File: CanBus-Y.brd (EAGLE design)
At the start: 58.4 x 15.9 mm, 3 parts

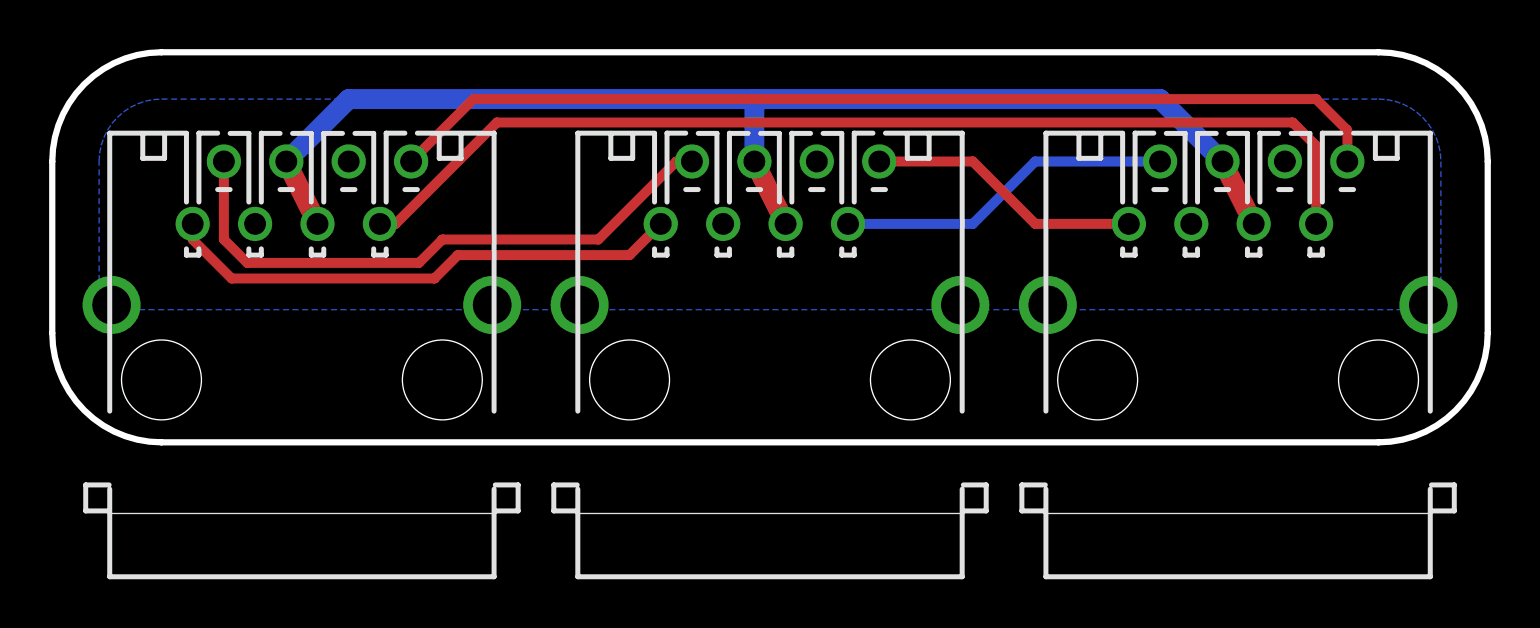
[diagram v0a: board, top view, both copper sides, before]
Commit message: Layouts angepasst, Backplane vergrößert
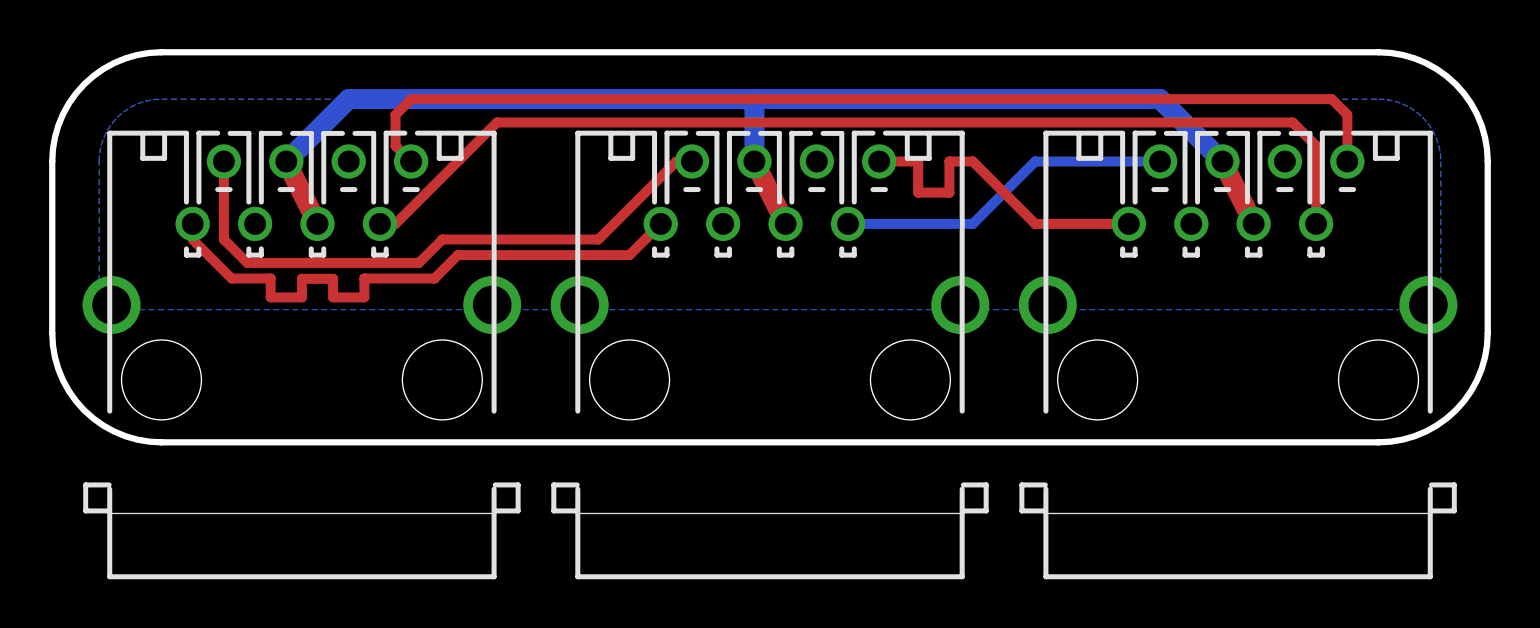
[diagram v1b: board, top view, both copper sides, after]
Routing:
- net CANL_1-2: track 21.3 -> 24.3 mm
- net CANL_2-3: track 11.2 -> 13.8 mm
- net CANL_3-1: track 40.9 -> 43.3 mm
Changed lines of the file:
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@@
 <wire x1="50.8" y1="8.89" x2="50.8" y2="12.065" width="0.4064" layer="1"/>
 <wire x1="50.8" y1="12.065" x2="49.8475" y2="13.0175" width="0.4064" layer="1"/>
-<wire x1="17.4625" y1="13.0175" x2="49.8475" y2="13.0175" width="0.4064" layer="1"/>
+<wire x1="49.8475" y1="13.0175" x2="17.4625" y2="13.0175" width="0.4064" layer="1"/>
 <wire x1="17.4625" y1="13.0175" x2="13.335" y2="8.89" width="0.4064" layer="1"/>
 <wire x1="13.335" y1="8.89" x2="12.7" y2="8.89" width="0.4064" layer="1"/>
@@
 <contactref element="J3" pad="8"/>
 <contactref element="J1" pad="8"/>
-<wire x1="52.07" y1="11.43" x2="52.07" y2="12.7" width="0.4064" layer="1"/>
-<wire x1="52.07" y1="12.7" x2="50.8" y2="13.97" width="0.4064" layer="1"/>
-<wire x1="16.51" y1="13.97" x2="50.8" y2="13.97" width="0.4064" layer="1"/>
-<wire x1="16.51" y1="13.97" x2="13.97" y2="11.43" width="0.4064" layer="1"/>
+<wire x1="52.07" y1="13.335" x2="52.07" y2="11.43" width="0.4064" layer="1"/>
+<wire x1="52.07" y1="13.335" x2="51.435" y2="13.97" width="0.4064" layer="1"/>
+<wire x1="51.435" y1="13.97" x2="13.97" y2="13.97" width="0.4064" layer="1"/>
+<wire x1="13.97" y1="13.97" x2="13.335" y2="13.335" width="0.4064" layer="1"/>
+<wire x1="13.335" y1="13.335" x2="13.335" y2="12.065" width="0.4064" layer="1"/>
+<wire x1="13.335" y1="12.065" x2="13.97" y2="11.43" width="0.4064" layer="1"/>
 </signal>
 <signal name="CANL_1-2">
@@
 <wire x1="5.08" y1="8.89" x2="5.08" y2="8.255" width="0.4064" layer="1"/>
 <wire x1="5.08" y1="8.255" x2="6.6675" y2="6.6675" width="0.4064" layer="1"/>
-<wire x1="6.6675" y1="6.6675" x2="14.9225" y2="6.6675" width="0.4064" layer="1"/>
 <wire x1="14.9225" y1="6.6675" x2="15.875" y2="7.62" width="0.4064" layer="1"/>
 <wire x1="15.875" y1="7.62" x2="22.86" y2="7.62" width="0.4064" layer="1"/>
 <wire x1="22.86" y1="7.62" x2="24.13" y2="8.89" width="0.4064" layer="1"/>
+<wire x1="8.255" y1="6.6675" x2="6.6675" y2="6.6675" width="0.4064" layer="1"/>
+<wire x1="8.255" y1="5.89915" x2="8.255" y2="6.6675" width="0.4064" layer="1"/>
+<wire x1="9.525" y1="5.89915" x2="8.255" y2="5.89915" width="0.4064" layer="1"/>
+<wire x1="9.525" y1="5.89915" x2="9.525" y2="6.6548" width="0.4064" layer="1"/>
+<wire x1="10.795" y1="6.6548" x2="9.525" y2="6.6548" width="0.4064" layer="1"/>
+<wire x1="10.795" y1="6.6548" x2="10.795" y2="5.89915" width="0.4064" layer="1"/>
+<wire x1="10.795" y1="5.89915" x2="12.065" y2="5.89915" width="0.4064" layer="1"/>
+<wire x1="12.065" y1="5.89915" x2="12.065" y2="6.6675" width="0.4064" layer="1"/>
+<wire x1="12.065" y1="6.6675" x2="14.9225" y2="6.6675" width="0.4064" layer="1"/>
 </signal>
 <signal name="CANH_1-2">
@@
 <wire x1="6.35" y1="11.43" x2="6.35" y2="8.255" width="0.4064" layer="1"/>
 <wire x1="6.35" y1="8.255" x2="7.3025" y2="7.3025" width="0.4064" layer="1"/>
-<wire x1="7.3025" y1="7.3025" x2="14.2875" y2="7.3025" width="0.4064" layer="1"/>
+<wire x1="14.2875" y1="7.3025" x2="7.3025" y2="7.3025" width="0.4064" layer="1"/>
 <wire x1="14.2875" y1="7.3025" x2="15.24" y2="8.255" width="0.4064" layer="1"/>
 <wire x1="15.24" y1="8.255" x2="21.59" y2="8.255" width="0.4064" layer="1"/>
@@
 <contactref element="J2" pad="7"/>
 <contactref element="J3" pad="2"/>
-<wire x1="36.83" y1="8.89" x2="31.75" y2="8.89" width="0.4064" layer="16"/>
+<wire x1="31.75" y1="8.89" x2="36.83" y2="8.89" width="0.4064" layer="16"/>
 <wire x1="36.83" y1="8.89" x2="39.37" y2="11.43" width="0.4064" layer="16"/>
 <wire x1="39.37" y1="11.43" x2="44.45" y2="11.43" width="0.4064" layer="16"/>
@@
 <contactref element="J2" pad="8"/>
 <contactref element="J3" pad="1"/>
-<wire x1="36.83" y1="11.43" x2="33.02" y2="11.43" width="0.4064" layer="1"/>
 <wire x1="36.83" y1="11.43" x2="39.37" y2="8.89" width="0.4064" layer="1"/>
 <wire x1="39.37" y1="8.89" x2="43.18" y2="8.89" width="0.4064" layer="1"/>
+<wire x1="33.02" y1="11.43" x2="34.6075" y2="11.43" width="0.4064" layer="1"/>
+<wire x1="34.6075" y1="11.43" x2="34.6075" y2="10.16" width="0.4064" layer="1"/>
+<wire x1="35.8775" y1="10.16" x2="34.6075" y2="10.16" width="0.4064" layer="1"/>
+<wire x1="35.8775" y1="10.16" x2="35.8775" y2="11.43" width="0.4064" layer="1"/>
+<wire x1="35.8775" y1="11.43" x2="36.83" y2="11.43" width="0.4064" layer="1"/>
 </signal>
 </signals>

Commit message: Layouts angepasst
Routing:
- net +24V: track 51.3 -> 52.8 mm
- added copper zone on layer 16, net BOT
- added copper zone on layer 1, net TOP
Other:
- board size 58.4 x 15.9 mm -> 58.4 x 18.7 mm
- board text added: "BOT"
- board text added: "TOP"

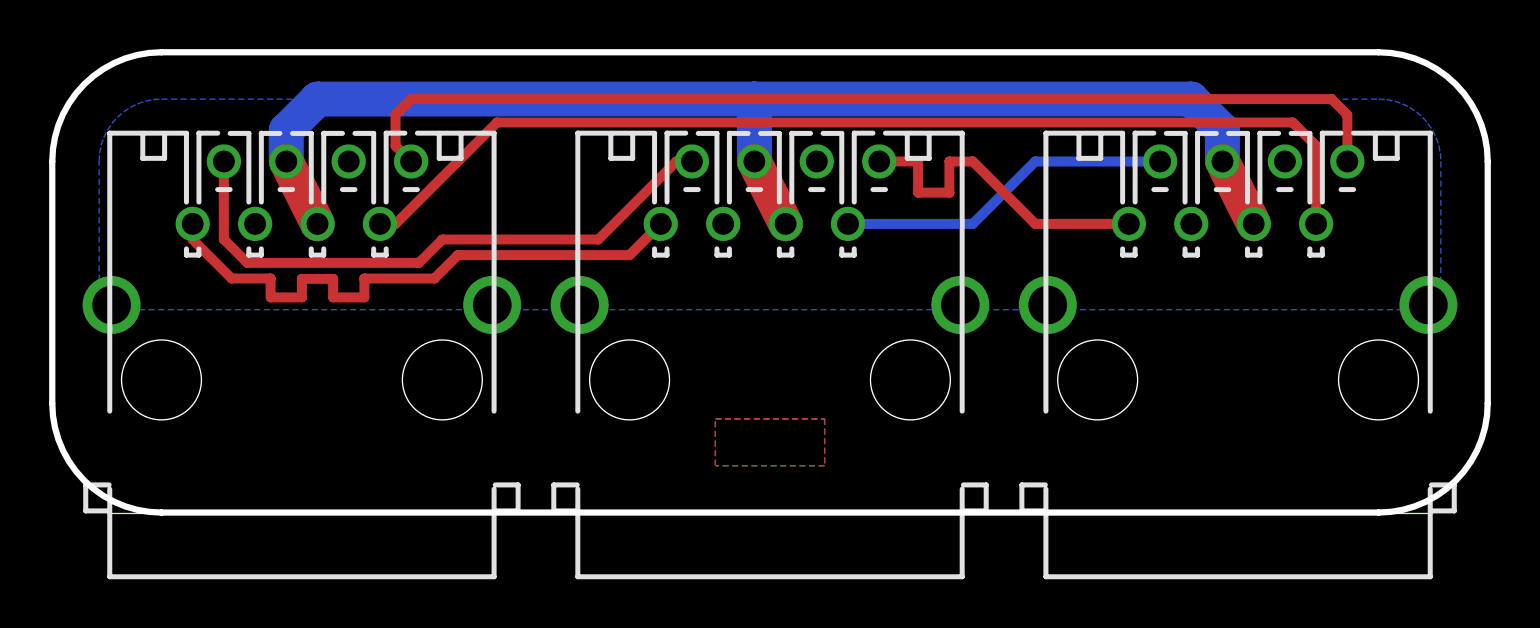
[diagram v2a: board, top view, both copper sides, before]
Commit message: Leiterplatten verkleinert zur Kostenerspranis
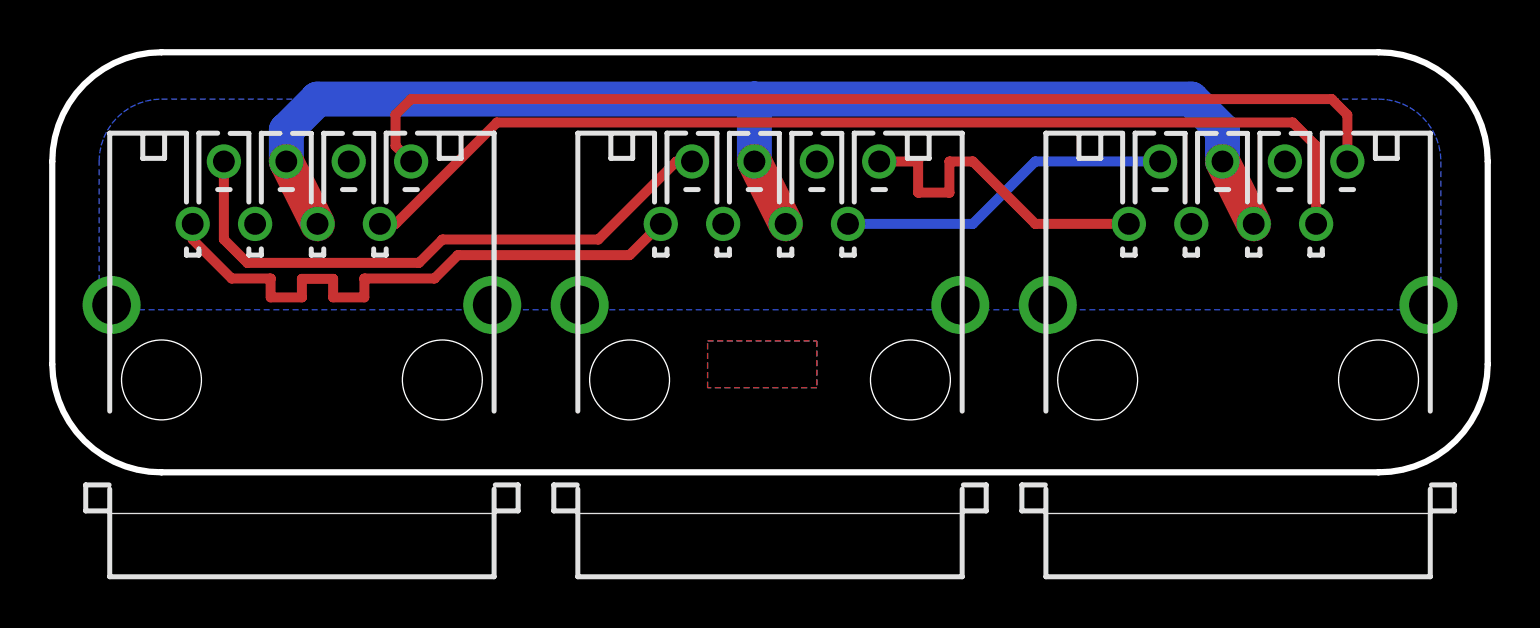
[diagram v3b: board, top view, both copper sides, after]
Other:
- board size 58.4 x 18.7 mm -> 58.4 x 17.1 mm
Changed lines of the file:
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@@
 <text x="28.575" y="5.715" size="1.016" layer="26" font="vector" ratio="15" rot="SMR0" align="center">CAN-Bus
 Y-Verteiler</text>
-<text x="9.525" y="2.54" size="1.27" layer="26" rot="SMR0" align="center">1</text>
-<text x="28.575" y="2.54" size="1.27" layer="26" rot="SMR0" align="center">2</text>
-<text x="47.625" y="2.54" size="1.27" layer="26" rot="SMR0" align="center">3</text>
+<text x="9.525" y="1.27" size="1.27" layer="26" rot="SMR0" align="center">1</text>
+<text x="28.575" y="1.27" size="1.27" layer="26" rot="SMR0" align="center">2</text>
+<text x="47.625" y="1.27" size="1.27" layer="26" rot="SMR0" align="center">3</text>
 <wire x1="-0.635" y1="11.43" x2="3.81" y2="15.875" width="0.254" layer="20" curve="-90"/>
 <wire x1="3.81" y1="15.875" x2="53.34" y2="15.875" width="0.254" layer="20"/>
 <wire x1="53.34" y1="15.875" x2="57.785" y2="11.43" width="0.254" layer="20" curve="-90"/>
-<wire x1="57.785" y1="11.43" x2="57.785" y2="1.5875" width="0.254" layer="20"/>
-<wire x1="57.785" y1="1.5875" x2="53.34" y2="-2.8575" width="0.254" layer="20" curve="-90"/>
-<wire x1="53.34" y1="-2.8575" x2="3.81" y2="-2.8575" width="0.254" layer="20"/>
-<wire x1="3.81" y1="-2.8575" x2="-0.635" y2="1.5875" width="0.254" layer="20" curve="-90"/>
-<wire x1="-0.635" y1="1.5875" x2="-0.635" y2="11.43" width="0.254" layer="20"/>
-<dimension x1="-0.635" y1="1.5875" x2="57.785" y2="1.5875" x3="28.575" y3="-13.0175" textsize="1.778" textratio="15" layer="47"/>
-<dimension x1="3.81" y1="-2.8575" x2="3.81" y2="15.875" x3="-3.81" y3="6.50875" textsize="1.778" textratio="15" layer="47"/>
-<text x="30.1625" y="-0.635" size="1.27" layer="42" font="vector" ratio="15" rot="MR0">BOT</text>
-<text x="30.1625" y="-0.635" size="1.27" layer="41" font="vector" ratio="15" align="bottom-right">TOP</text>
+<wire x1="57.785" y1="11.43" x2="57.785" y2="3.18" width="0.254" layer="20"/>
+<wire x1="57.785" y1="3.18" x2="53.34" y2="-1.22" width="0.254" layer="20" curve="-90"/>
+<wire x1="53.34" y1="-1.22" x2="3.81" y2="-1.22" width="0.254" layer="20"/>
+<wire x1="3.81" y1="-1.22" x2="-0.635" y2="3.18" width="0.254" layer="20" curve="-90"/>
+<wire x1="-0.635" y1="3.18" x2="-0.635" y2="11.43" width="0.254" layer="20"/>
+<dimension x1="-0.635" y1="3.175" x2="57.785" y2="3.175" x3="28.575" y3="-13.0175" textsize="1.778" textratio="15" layer="47"/>
+<dimension x1="3.81" y1="-1.22" x2="3.81" y2="15.875" x3="-3.81" y3="7.3275" textsize="1.778" textratio="15" layer="47"/>
+<text x="26.67" y="3.81" size="1.27" layer="42" font="vector" ratio="15" rot="MR180">BOT</text>
+<text x="26.67" y="3.81" size="1.27" layer="41" font="vector" ratio="15" rot="R180" align="bottom-right">TOP</text>
 </plain>
 <attributes>
@@
 <signal name="TOP">
 <polygon width="0.254" layer="1" orphans="yes">
-<vertex x="26.3525" y="0.9525"/>
-<vertex x="30.7975" y="0.9525"/>
-<vertex x="30.7975" y="-0.9525"/>
-<vertex x="26.3525" y="-0.9525"/>
+<vertex x="30.48" y="2.2225"/>
+<vertex x="26.035" y="2.2225"/>
+<vertex x="26.035" y="4.1275"/>
+<vertex x="30.48" y="4.1275"/>
 </polygon>
 </signal>
 <signal name="BOT">
 <polygon width="0.254" layer="16" orphans="yes">
-<vertex x="26.3525" y="0.9525"/>
-<vertex x="30.7975" y="0.9525"/>
-<vertex x="30.7975" y="-0.9525"/>
-<vertex x="26.3525" y="-0.9525"/>
+<vertex x="30.48" y="2.2225"/>
+<vertex x="26.035" y="2.2225"/>
+<vertex x="26.035" y="4.1275"/>
+<vertex x="30.48" y="4.1275"/>
 </polygon>
 </signal>
